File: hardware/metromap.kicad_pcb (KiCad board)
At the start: 4 copper layers, 100 x 100 mm, 160 parts, among them J1 USB_C_Receptacle_USB2.0_16P, U1 AZ1117-3.3, U2 SN74LVC1G125DBV, U3 ESP32-C6-MINI-1-H4

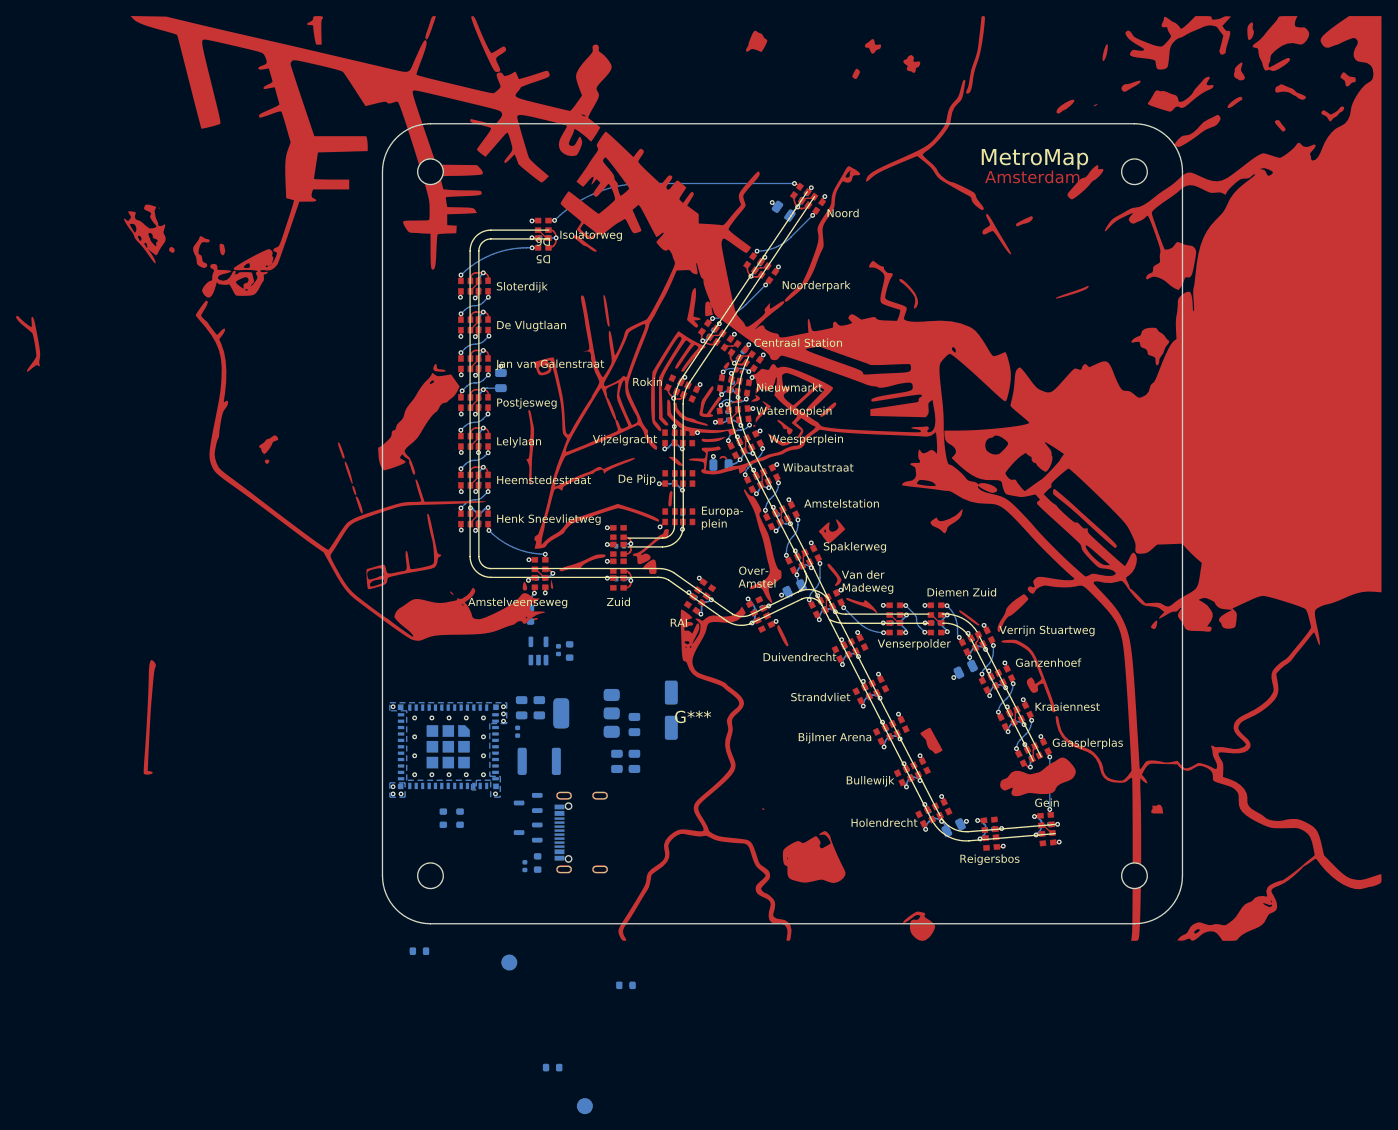
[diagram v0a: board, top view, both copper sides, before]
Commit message: Updated LED footprint
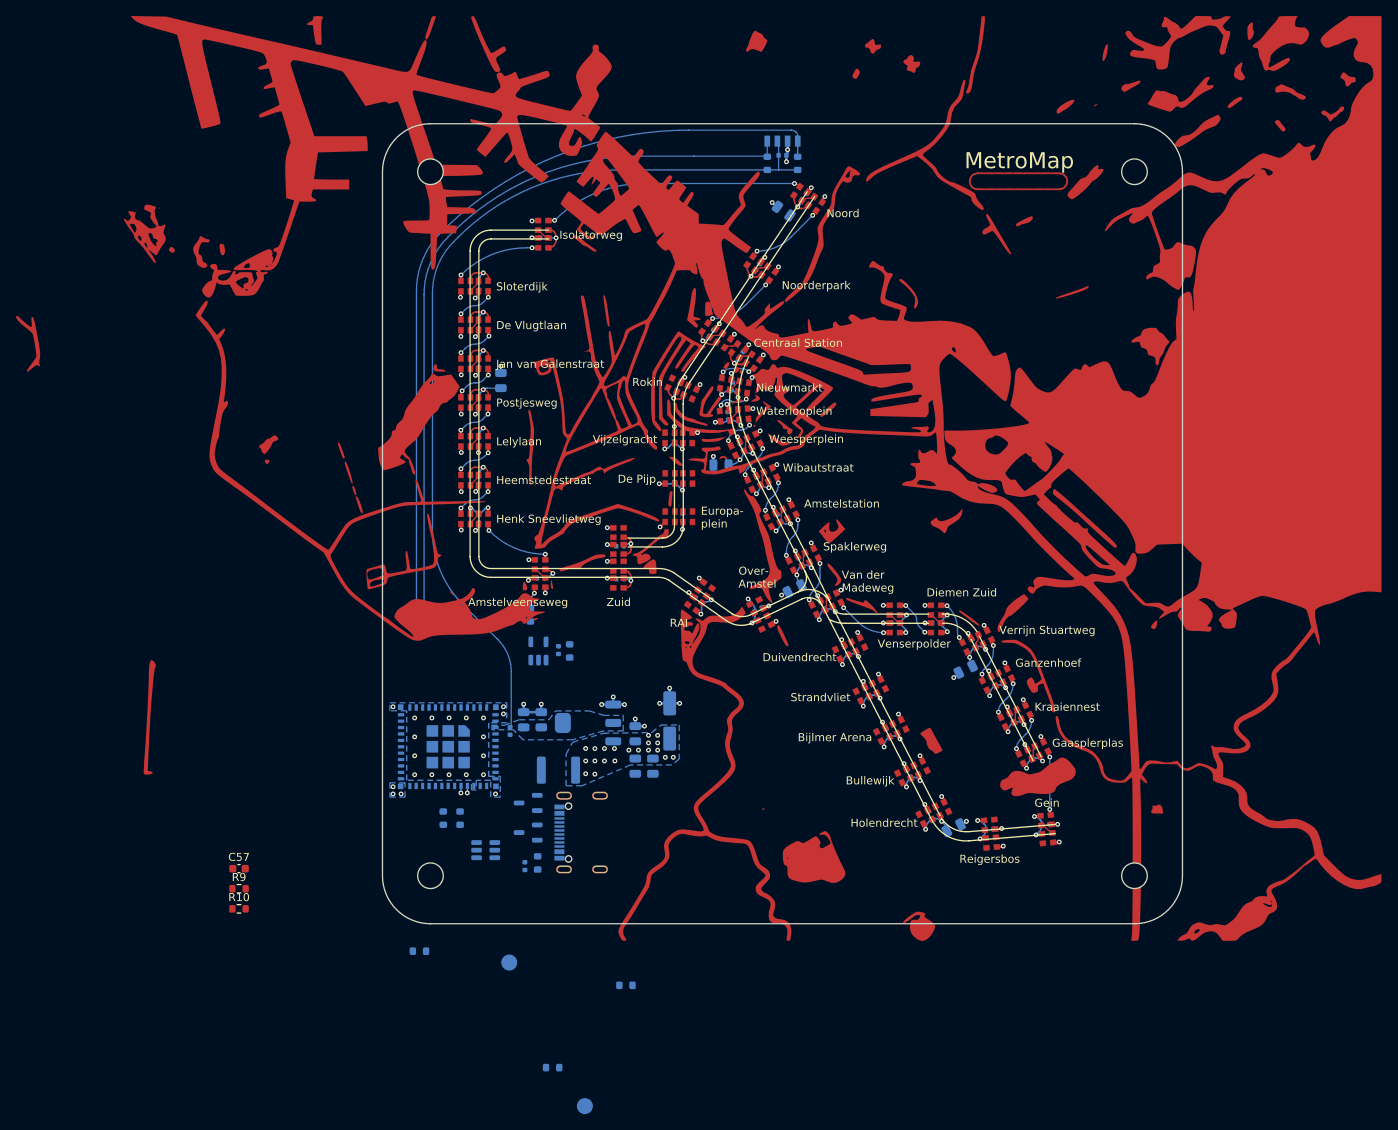
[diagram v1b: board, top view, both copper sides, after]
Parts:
- added C57: 1u, Capacitor_SMD:C_0603_1608Metric, F.Cu at (44.3, 122.1)
- added C58: 100n, Capacitor_SMD:C_0402_1005Metric, B.Cu at (112.2, 33.0)
- added R10: 10k, Resistor_SMD:R_0603_1608Metric, F.Cu at (44.3, 127.1)
- added R11: 4k7, Resistor_SMD:R_0603_1608Metric, B.Cu at (114.1, 34.0)
- added R12: 4k7, Resistor_SMD:R_0603_1608Metric, B.Cu at (110.3, 34.0)
- added R9: 1k, Resistor_SMD:R_0603_1608Metric, F.Cu at (44.3, 124.6)
- added U4: CH221K, Package_TO_SOT_SMD:SOT-23-6, B.Cu at (75.1, 119.8)
- added U5: VEML7700-TR, metro-tracker:XDCR_VEML7700-TR, B.Cu at (112.2, 30.5)
- moved F1 2.64 mm to (84.2, 109.8)
- moved C10 2.38 mm to (93.8, 109.3)
- moved C9 2.38 mm to (96.0, 109.3)
- moved C11 1.52 mm to (79.8, 103.5)
- moved C12 1.52 mm to (82.0, 103.5)
- moved C8 1.36 mm to (98.1, 103.7)
- moved U1 1.22 mm to (87.9, 103.9)
- moved C5 1.15 mm to (93.8, 105.2)
- moved C13 0.96 mm to (78.2, 104.9)
- turned D10 to 90 degrees
- turned D11 to -125 degrees
- turned D12 to -64 degrees
- turned D13 to -90 degrees
- turned D14 to -64 degrees
- turned D15 to -175 degrees
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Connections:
- D10 pad 1: GND -> +5V
- D10 pad 3: +5V -> GND
- D11 pad 1: GND -> +5V
- D11 pad 3: +5V -> GND
- D12 pad 1: GND -> +5V
- D12 pad 3: +5V -> GND
- D13 pad 1: GND -> +5V
- D13 pad 3: +5V -> GND
- D14 pad 1: GND -> +5V
- D14 pad 3: +5V -> GND
- D15 pad 1: GND -> +5V
- D15 pad 3: +5V -> GND
- D16 pad 1: GND -> +5V
- D16 pad 2: Net-(D16-DIN) -> unconnected-(D16-DOUT-Pad2)
- D16 pad 3: +5V -> GND
- D16 pad 4: unconnected-(D16-DOUT-Pad4) -> Net-(D16-DIN)
- D17 pad 1: GND -> +5V
- D17 pad 3: +5V -> GND
- D18 pad 1: GND -> +5V
- D18 pad 3: +5V -> GND
- D19 pad 1: GND -> +5V
- D19 pad 2: Net-(D19-DIN) -> Net-(D16-DIN)
- D19 pad 3: +5V -> GND
- D19 pad 4: Net-(D16-DIN) -> Net-(D19-DOUT)
- D20 pad 1: GND -> +5V
- D20 pad 2: Net-(D10-DOUT) -> Net-(D20-DIN)
- D20 pad 3: +5V -> GND
- D20 pad 4: Net-(D20-DOUT) -> Net-(D10-DIN)
- D21 pad 1: GND -> +5V
- D21 pad 2: Net-(D20-DOUT) -> Net-(D21-DIN)
- D21 pad 3: +5V -> GND
- D21 pad 4: Net-(D21-DOUT) -> Net-(D20-DIN)
- D22 pad 1: GND -> +5V
- D22 pad 2: Net-(D11-DOUT) -> Net-(D22-DIN)
- D22 pad 3: +5V -> GND
- D22 pad 4: Net-(D22-DOUT) -> Net-(D11-DIN)
- D23 pad 1: GND -> +5V
- D23 pad 2: Net-(D22-DOUT) -> Net-(D23-DIN)
- D23 pad 3: +5V -> GND
- D23 pad 4: Net-(D23-DOUT) -> Net-(D22-DIN)
- D24 pad 1: GND -> +5V
- D24 pad 2: Net-(D23-DOUT) -> Net-(D24-DIN)
- D24 pad 3: +5V -> GND
- D24 pad 4: Net-(D24-DOUT) -> Net-(D23-DIN)
- D25 pad 1: GND -> +5V
- D25 pad 2: Net-(D21-DOUT) -> Net-(D25-DIN)
- D25 pad 3: +5V -> GND
- D25 pad 4: Net-(D25-DOUT) -> Net-(D21-DIN)
- D26 pad 1: GND -> +5V
- D26 pad 2: Net-(D25-DOUT) -> Net-(D26-DIN)
- D26 pad 3: +5V -> GND
- D26 pad 4: Net-(D26-DOUT) -> Net-(D25-DIN)
- D27 pad 1: GND -> +5V
- D27 pad 3: +5V -> GND
- D28 pad 1: GND -> +5V
- D28 pad 3: +5V -> GND
- D29 pad 1: GND -> +5V
- D29 pad 2: Net-(D24-DOUT) -> Net-(D27-DOUT)
- D29 pad 3: +5V -> GND
- D29 pad 4: Net-(D27-DIN) -> Net-(D24-DIN)
- D3 pad 1: GND -> +5V
- D3 pad 3: +5V -> GND
- D30 pad 1: GND -> +5V
- D30 pad 3: +5V -> GND
- D31 pad 1: GND -> +5V
- D31 pad 2: Net-(D26-DOUT) -> Net-(D31-DIN)
- D31 pad 3: +5V -> GND
- D31 pad 4: Net-(D31-DOUT) -> Net-(D26-DIN)
- D32 pad 1: GND -> +5V
- D32 pad 2: Net-(D31-DOUT) -> Net-(D32-DIN)
- D32 pad 3: +5V -> GND
- D32 pad 4: Net-(D32-DOUT) -> Net-(D31-DIN)
- D33 pad 1: GND -> +5V
- D33 pad 3: +5V -> GND
- D34 pad 1: GND -> +5V
- D34 pad 2: Net-(D27-DOUT) -> Net-(D33-DOUT)
- D34 pad 3: +5V -> GND
- D34 pad 4: Net-(D33-DIN) -> Net-(D27-DIN)
- D35 pad 1: GND -> +5V
- D35 pad 3: +5V -> GND
- D36 pad 1: GND -> +5V
- D36 pad 3: +5V -> GND
- D37 pad 1: GND -> +5V
- D37 pad 3: +5V -> GND
- D38 pad 1: GND -> +5V
- D38 pad 3: +5V -> GND
- D39 pad 1: GND -> +5V
- D39 pad 2: Net-(D38-DOUT) -> Net-(D39-DIN)
- D39 pad 3: +5V -> GND
- D39 pad 4: Net-(D39-DOUT) -> Net-(D38-DIN)
- D4 pad 1: GND -> +5V
- D4 pad 2: Net-(D3-DOUT) -> Net-(D4-DIN)
- D4 pad 3: +5V -> GND
- D4 pad 4: Net-(D4-DOUT) -> Net-(D3-DIN)
- D40 pad 1: GND -> +5V
- D40 pad 2: Net-(D35-DOUT) -> Net-(D12-DOUT)
- D40 pad 3: +5V -> GND
- D40 pad 4: Net-(D12-DIN) -> Net-(D35-DIN)
- D41 pad 1: GND -> +5V
- D41 pad 3: +5V -> GND
- D42 pad 1: GND -> +5V
- D42 pad 2: Net-(D39-DOUT) -> Net-(D42-DIN)
- D42 pad 3: +5V -> GND
- D42 pad 4: Net-(D42-DOUT) -> Net-(D39-DIN)
- D43 pad 1: GND -> +5V
- D43 pad 2: Net-(D42-DOUT) -> Net-(D43-DIN)
- D43 pad 3: +5V -> GND
- D43 pad 4: Net-(D43-DOUT) -> Net-(D42-DIN)
- D44 pad 1: GND -> +5V
- D44 pad 3: +5V -> GND
- D45 pad 1: GND -> +5V
- D45 pad 3: +5V -> GND
- D46 pad 1: GND -> +5V
- D46 pad 2: Net-(D12-DOUT) -> Net-(D41-DOUT)
- D46 pad 3: +5V -> GND
- D46 pad 4: Net-(D41-DIN) -> Net-(D12-DIN)
- D47 pad 1: GND -> +5V
- D47 pad 3: +5V -> GND
- D48 pad 1: GND -> +5V
- D48 pad 3: +5V -> GND
- D49 pad 1: GND -> +5V
- D49 pad 3: +5V -> GND
- D5 pad 1: GND -> +5V
- D5 pad 2: Net-(D43-DOUT) -> Net-(D5-DIN)
- D5 pad 3: +5V -> GND
- D5 pad 4: Net-(D5-DOUT) -> Net-(D43-DIN)
- D50 pad 1: GND -> +5V
- D50 pad 3: +5V -> GND
- D51 pad 1: GND -> +5V
- D51 pad 3: +5V -> GND
- D52 pad 1: GND -> +5V
- D52 pad 2: Net-(D41-DOUT) -> Net-(D49-DOUT)
- D52 pad 3: +5V -> GND
- D52 pad 4: Net-(D49-DIN) -> Net-(D41-DIN)
- D53 pad 1: GND -> +5V
- D53 pad 3: +5V -> GND
- D54 pad 1: GND -> +5V
- D54 pad 3: +5V -> GND
- D55 pad 1: GND -> +5V
- D55 pad 2: Net-(D54-DOUT) -> Net-(D55-DIN)
- D55 pad 3: +5V -> GND
- D55 pad 4: Net-(D55-DOUT) -> Net-(D54-DIN)
- D56 pad 1: GND -> +5V
- D56 pad 3: +5V -> GND
- D57 pad 1: GND -> +5V
- D57 pad 2: Net-(D57-DIN) -> Net-(D54-DOUT)
- D57 pad 3: +5V -> GND
- D57 pad 4: Net-(D54-DIN) -> Net-(D57-DOUT)
- D58 pad 1: GND -> +5V
- D58 pad 2: Net-(D55-DOUT) -> Net-(D58-DIN)
- D58 pad 3: +5V -> GND
- D58 pad 4: Net-(D58-DOUT) -> Net-(D55-DIN)
- D59 pad 1: GND -> +5V
- D59 pad 3: +5V -> GND
- D6 pad 1: GND -> +5V
- D6 pad 2: Net-(D5-DOUT) -> Net-(D3-DOUT)
- D6 pad 3: +5V -> GND
- D6 pad 4: Net-(D3-DIN) -> Net-(D5-DIN)
- D60 pad 1: GND -> +5V
- D60 pad 3: +5V -> GND
- D61 pad 1: GND -> +5V
- D61 pad 2: Net-(D58-DOUT) -> Net-(D59-DOUT)
- D61 pad 3: +5V -> GND
- D61 pad 4: Net-(D59-DIN) -> Net-(D58-DIN)
- D62 pad 1: GND -> +5V
- D62 pad 3: +5V -> GND
- D63 pad 1: GND -> +5V
- D63 pad 3: +5V -> GND
- D64 pad 1: GND -> +5V
- D64 pad 2: Net-(D59-DOUT) -> Net-(D63-DOUT)
- D64 pad 3: +5V -> GND
- D64 pad 4: Net-(D63-DIN) -> Net-(D59-DIN)
- D65 pad 1: GND -> +5V
- D65 pad 3: +5V -> GND
- D66 pad 1: GND -> +5V
- D66 pad 3: +5V -> GND
- D67 pad 1: GND -> +5V
- D67 pad 3: +5V -> GND
- D68 pad 1: GND -> +5V
- D68 pad 2: Net-(D63-DOUT) -> Net-(D67-DOUT)
- D68 pad 3: +5V -> GND
- D68 pad 4: Net-(D67-DIN) -> Net-(D63-DIN)
- D69 pad 1: GND -> +5V
- D69 pad 3: +5V -> GND
- D7 pad 1: GND -> +5V
- D7 pad 2: Net-(D4-DOUT) -> Net-(D7-DIN)
- D7 pad 3: +5V -> GND
- D7 pad 4: Net-(D7-DOUT) -> Net-(D4-DIN)
- D70 pad 1: GND -> +5V
- D70 pad 3: +5V -> GND
- D71 pad 1: GND -> +5V
- D71 pad 2: Net-(D49-DOUT) -> Net-(D71-DIN)
- D71 pad 3: +5V -> GND
- D71 pad 4: Net-(D71-DOUT) -> Net-(D49-DIN)
- D72 pad 1: GND -> +5V
- D72 pad 2: Net-(D33-DOUT) -> Net-(D35-DOUT)
- D72 pad 3: +5V -> GND
- D72 pad 4: Net-(D35-DIN) -> Net-(D33-DIN)
- D73 pad 1: GND -> +5V
- D73 pad 2: Net-(D32-DOUT) -> Net-(D73-DIN)
- D73 pad 3: +5V -> GND
- D73 pad 4: Net-(D73-DOUT) -> Net-(D32-DIN)
- D74 pad 1: GND -> +5V
- D74 pad 2: Net-(D73-DOUT) -> Net-(D38-DOUT)
- D74 pad 3: +5V -> GND
- D74 pad 4: Net-(D38-DIN) -> Net-(D73-DIN)
- D75 pad 1: GND -> +5V
- D75 pad 2: Net-(D67-DOUT) -> Net-(D75-DIN)
- D75 pad 3: +5V -> GND
- D75 pad 4: Net-(D75-DOUT) -> Net-(D67-DIN)
- D76 pad 1: GND -> +5V
- D76 pad 3: +5V -> GND
- D77 pad 1: GND -> +5V
- D77 pad 3: +5V -> GND
- D78 pad 1: GND -> +5V
- D78 pad 3: +5V -> GND
- D79 pad 1: GND -> +5V
- D79 pad 2: Net-(D71-DOUT) -> Net-(D57-DOUT)
- D79 pad 3: +5V -> GND
- D79 pad 4: Net-(D57-DIN) -> Net-(D71-DIN)
- D8 pad 1: GND -> +5V
- D8 pad 2: Net-(D7-DOUT) -> Net-(D11-DOUT)
- D8 pad 3: +5V -> GND
- D8 pad 4: Net-(D11-DIN) -> Net-(D7-DIN)
- D80 pad 1: GND -> +5V
- D80 pad 3: +5V -> GND
- D81 pad 1: GND -> +5V
- D81 pad 2: Net-(D75-DOUT) -> Net-(D19-DOUT)
- D81 pad 3: +5V -> GND
- D81 pad 4: Net-(D19-DIN) -> Net-(D75-DIN)
- D82 pad 1: GND -> +5V
- D82 pad 2: /LEDs/DATA_IN -> Net-(D50-DOUT)
- D82 pad 3: +5V -> GND
- D82 pad 4: Net-(D50-DIN) -> /LEDs/DATA_IN
- D83 pad 1: GND -> +5V
- D83 pad 3: +5V -> GND
- D84 pad 1: GND -> +5V
- D84 pad 3: +5V -> GND
- D9 pad 1: GND -> +5V
- D9 pad 2: Net-(D50-DOUT) -> Net-(D10-DOUT)
- D9 pad 3: +5V -> GND
- D9 pad 4: Net-(D10-DIN) -> Net-(D50-DIN)
- U3 pad 15: unconnected-(U3-IO6-Pad15) -> /SDA
- U3 pad 16: unconnected-(U3-IO7-Pad16) -> /SCL
- U3 pad 29: unconnected-(U3-IO23-Pad29) -> /TOUCH
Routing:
- net +3.3V: track 0.00 -> 113.6 mm
- net /SDA: track 0.00 -> 102.4 mm, vias 0 -> 1
- net /SCL: track 0.00 -> 95.3 mm, vias 0 -> 1
- net Net-(D3-DOUT): track 1.65 -> 32.7 mm, vias 0 -> 2
- net Net-(D3-DIN): track 32.7 -> 1.65 mm, vias 2 -> 0
- net GND: track 104.8 -> 121.9 mm, vias 106 -> 117
- net Net-(D43-DOUT): track 11.2 -> 0.00 mm, vias 2 -> 0
- net Net-(D43-DIN): track 0.00 -> 11.2 mm, vias 0 -> 2
- net Net-(D4-DOUT): track 10.1 -> 0.00 mm, vias 2 -> 0
- net Net-(D4-DIN): track 0.00 -> 10.1 mm, vias 0 -> 2
- net Net-(D19-DOUT): track 0.00 -> 8.04 mm, vias 0 -> 2
- net Net-(D19-DIN): track 8.04 -> 0.00 mm, vias 2 -> 0
- net Net-(D11-DOUT): track 1.74 -> 9.67 mm, vias 0 -> 2
- net Net-(D11-DIN): track 9.67 -> 1.74 mm, vias 2 -> 0
- net Net-(D57-DOUT): track 0.00 -> 7.73 mm, vias 0 -> 2
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- added copper zone on B.Cu, net +3.3V
- added copper zone on B.Cu, net +5V
- added copper zone on F.Cu, net /TOUCH

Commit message: replaced buffer
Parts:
- added TP3: ~, TestPoint:TestPoint_Pad_D2.0mm, B.Cu at (83.8, 91.2)
- added TP4: ~, TestPoint:TestPoint_Pad_D2.0mm, B.Cu at (88.2, 95.7)
- C57, R10, R9: moved to B.Cu
- U2: value SN74LVC1G125DBV -> SN74AHCT1G125DBVR
- moved R1 38.7 mm to (79.0, 108.5)
- moved C57 35.3 mm to (79.3, 125.5)
- moved R9 35.1 mm to (79.3, 123.8), turned to 180 degrees
- moved R10 31.8 mm to (75.9, 123.8), turned to 180 degrees
- moved TP2 26.7 mm to (90.5, 125.2)
- moved R3 19.8 mm to (80.6, 121.0), turned to -90 degrees
- moved R4 16.7 mm to (79.0, 121.0), turned to -90 degrees
- moved TP1 9.82 mm to (82.8, 125.2)
- moved C15 8.54 mm to (88.0, 124.7), turned to -90 degrees
- moved R8 6.14 mm to (86.7, 124.9), turned to -90 degrees
- moved R7 4.90 mm to (74.7, 116.2), turned to 180 degrees
- moved R5 3.02 mm to (74.7, 114.7), turned to 180 degrees
- moved U4 1.47 mm to (76.0, 121.0)
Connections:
- net /~{OE_EN} renamed /~{OE}
- D2 pad 1: Net-(D2-K-Pad1) -> /CON_USB_D-
- D2 pad 2: Net-(D2-K-Pad2) -> /CON_USB_D+
- J1 pad A6: Net-(D2-K-Pad1) -> /CON_USB_D+
- J1 pad A7: Net-(D2-K-Pad2) -> /CON_USB_D-
- J1 pad B6: Net-(D2-K-Pad1) -> /CON_USB_D+
- J1 pad B7: Net-(D2-K-Pad2) -> /CON_USB_D-
- R5 pad 1: Net-(D2-K-Pad2) -> /CON_USB_D-
- R7 pad 1: Net-(D2-K-Pad1) -> /CON_USB_D+
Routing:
- net /SDA: track 102.4 -> 131.2 mm, vias 1 -> 2
- net /~{OE}: track 0.00 -> 27.8 mm, vias 0 -> 2
- net /SCL: track 95.3 -> 121.8 mm, vias 1 -> 2
- net Net-(D1-K-Pad1): track 0.00 -> 24.8 mm
- net /LED_DATA: track 0.00 -> 22.0 mm, vias 0 -> 2
- net GND: track 121.9 -> 141.1 mm, vias 117 -> 133
- net /CON_USB_D+: track 0.00 -> 13.6 mm
- net /CON_USB_D-: track 0.00 -> 12.7 mm
- net Net-(J1-CC1): track 0.00 -> 9.36 mm, vias 0 -> 2
- net Net-(U4-VDD): track 0.00 -> 7.98 mm
- net Net-(J1-CC2): track 0.00 -> 7.92 mm
- net /USB_D+: track 0.00 -> 6.76 mm
- net /USB_D-: track 0.00 -> 5.96 mm
- net Net-(R6-Pad1): track 0.00 -> 5.58 mm
- net +3.3V: track 113.6 -> 117.8 mm
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- removed copper zone on F.Cu, net /TOUCH
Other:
- board text added: "DATA_IN"
- board text added: "Europa plein"
- board text added: "GND"
- board text added: "Over amstel"
- board text added: "VBUS"
- board text added: "~{OE}"
- board text removed: "Europa- plein"
- board text removed: "Over- Amstel"

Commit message: Initial routing done
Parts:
- added C59: 47u, Capacitor_SMD:CP_Elec_6.3x7.7, B.Cu at (101.6, 105.8)
- C8: footprint Capacitor_SMD:CP_Elec_5x5.7 -> Capacitor_SMD:CP_Elec_6.3x7.7
- moved C8 6.14 mm to (101.6, 98.6), turned to 0 degrees
- moved C2 3.42 mm to (134.0, 113.6), turned to -64 degrees
- moved TP2 2.55 mm to (93.0, 125.2)
- moved D60 2.33 mm to (119.5, 95.1), turned to 116 degrees
- moved D77 2.32 mm to (129.6, 109.6), turned to 116 degrees
- moved D14 2.31 mm to (132.2, 114.8), turned to 116 degrees
- moved D70 2.27 mm to (126.9, 104.5), turned to 116 degrees
- moved D18 2.26 mm to (130.2, 115.8), turned to 116 degrees
- moved D65 2.26 mm to (122.2, 100.3), turned to 116 degrees
- moved D78 2.23 mm to (101.3, 89.0), turned to 145 degrees
- moved D84 2.22 mm to (102.5, 87.2), turned to 145 degrees
- moved D69 2.22 mm to (124.9, 105.5), turned to 116 degrees
- moved D66 2.21 mm to (124.2, 99.3), turned to 116 degrees
- moved D76 2.20 mm to (127.5, 110.6), turned to 116 degrees
- moved D62 2.10 mm to (121.5, 94.2), turned to 116 degrees
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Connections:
- net Net-(D1-K-Pad1) renamed /VBUS
- net Net-(J1-SHIELD) renamed /SH
- D13 pad 2: unconnected-(D13-DOUT-Pad2) -> Net-(D13-DOUT)
- D13 pad 4: unconnected-(D13-DIN-Pad4) -> Net-(D13-DIN)
- D14 pad 2: unconnected-(D14-DOUT-Pad2) -> Net-(D14-DOUT)
- D14 pad 4: unconnected-(D14-DIN-Pad4) -> Net-(D14-DIN)
- D15 pad 2: unconnected-(D15-DOUT-Pad2) -> Net-(D15-DOUT)
- D15 pad 4: unconnected-(D15-DIN-Pad4) -> Net-(D15-DIN)
- D16 pad 2: unconnected-(D16-DOUT-Pad2) -> Net-(D15-DIN)
- D17 pad 2: unconnected-(D17-DOUT-Pad2) -> Net-(D14-DIN)
- D17 pad 4: unconnected-(D17-DIN-Pad4) -> Net-(D15-DOUT)
- D18 pad 2: unconnected-(D18-DOUT-Pad2) -> Net-(D18-DOUT)
- D18 pad 4: unconnected-(D18-DIN-Pad4) -> Net-(D14-DOUT)
- D28 pad 2: unconnected-(D28-DOUT-Pad2) -> Net-(D28-DOUT)
- D28 pad 4: unconnected-(D28-DIN-Pad4) -> Net-(D28-DIN)
- D30 pad 2: unconnected-(D30-DOUT-Pad2) -> Net-(D30-DOUT)
- D30 pad 4: unconnected-(D30-DIN-Pad4) -> Net-(D28-DOUT)
- D36 pad 2: unconnected-(D36-DOUT-Pad2) -> Net-(D36-DOUT)
- D36 pad 4: unconnected-(D36-DIN-Pad4) -> Net-(D30-DOUT)
- D37 pad 2: unconnected-(D37-DOUT-Pad2) -> Net-(D37-DOUT)
- D37 pad 4: unconnected-(D37-DIN-Pad4) -> Net-(D13-DOUT)
- D44 pad 2: unconnected-(D44-DOUT-Pad2) -> Net-(D44-DOUT)
- D44 pad 4: unconnected-(D44-DIN-Pad4) -> Net-(D37-DOUT)
- D45 pad 4: unconnected-(D45-DIN-Pad4) -> Net-(D44-DOUT)
- D47 pad 2: unconnected-(D47-DOUT-Pad2) -> Net-(D28-DIN)
- D47 pad 4: unconnected-(D47-DIN-Pad4) -> Net-(D47-DIN)
- D48 pad 2: unconnected-(D48-DOUT-Pad2) -> Net-(D47-DIN)
- D48 pad 4: unconnected-(D48-DIN-Pad4) -> Net-(D48-DIN)
- D51 pad 2: unconnected-(D51-DOUT-Pad2) -> Net-(D48-DIN)
- D51 pad 4: unconnected-(D51-DIN-Pad4) -> Net-(D51-DIN)
- D53 pad 2: unconnected-(D53-DOUT-Pad2) -> Net-(D51-DIN)
- D53 pad 4: unconnected-(D53-DIN-Pad4) -> Net-(D53-DIN)
- D56 pad 2: unconnected-(D56-DOUT-Pad2) -> Net-(D56-DOUT)
- D56 pad 4: unconnected-(D56-DIN-Pad4) -> Net-(D56-DIN)
- D60 pad 2: unconnected-(D60-DOUT-Pad2) -> Net-(D60-DOUT)
- D60 pad 4: unconnected-(D60-DIN-Pad4) -> Net-(D60-DIN)
- D62 pad 2: unconnected-(D62-DOUT-Pad2) -> Net-(D60-DIN)
- D62 pad 4: unconnected-(D62-DIN-Pad4) -> Net-(D62-DIN)
- D65 pad 2: unconnected-(D65-DOUT-Pad2) -> Net-(D62-DIN)
- D65 pad 4: unconnected-(D65-DIN-Pad4) -> Net-(D65-DIN)
- D66 pad 2: unconnected-(D66-DOUT-Pad2) -> Net-(D65-DIN)
- D66 pad 4: unconnected-(D66-DIN-Pad4) -> Net-(D66-DIN)
- D69 pad 2: unconnected-(D69-DOUT-Pad2) -> Net-(D66-DIN)
- D69 pad 4: unconnected-(D69-DIN-Pad4) -> Net-(D69-DIN)
- D70 pad 2: unconnected-(D70-DOUT-Pad2) -> Net-(D69-DIN)
- D70 pad 4: unconnected-(D70-DIN-Pad4) -> Net-(D70-DIN)
- D76 pad 2: unconnected-(D76-DOUT-Pad2) -> Net-(D70-DIN)
- D76 pad 4: unconnected-(D76-DIN-Pad4) -> Net-(D76-DIN)
- D77 pad 2: unconnected-(D77-DOUT-Pad2) -> Net-(D76-DIN)
- D77 pad 4: unconnected-(D77-DIN-Pad4) -> Net-(D18-DOUT)
- D78 pad 2: unconnected-(D78-DOUT-Pad2) -> Net-(D53-DIN)
- D78 pad 4: unconnected-(D78-DIN-Pad4) -> Net-(D78-DIN)
- D80 pad 2: unconnected-(D80-DOUT-Pad2) -> Net-(D56-DIN)
- D80 pad 4: unconnected-(D80-DIN-Pad4) -> Net-(D60-DOUT)
- D83 pad 2: unconnected-(D83-DOUT-Pad2) -> Net-(D13-DIN)
- D83 pad 4: unconnected-(D83-DIN-Pad4) -> Net-(D36-DOUT)
- D84 pad 2: unconnected-(D84-DOUT-Pad2) -> Net-(D78-DIN)
- D84 pad 4: unconnected-(D84-DIN-Pad4) -> Net-(D56-DOUT)
- U3 pad 29: /TOUCH -> unconnected-(U3-IO23-Pad29)
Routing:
- net Net-(D28-DIN): track 0.00 -> 22.3 mm, vias 0 -> 2
- net GND: track 141.1 -> 161.4 mm, vias 133 -> 145
- net Net-(D60-DOUT): track 0.00 -> 13.1 mm, vias 0 -> 2
- net Net-(D53-DIN): track 0.00 -> 11.5 mm, vias 0 -> 2
- net Net-(D56-DOUT): track 0.00 -> 8.94 mm, vias 0 -> 2
- net /VBUS: track 24.8 -> 16.4 mm
- net Net-(D30-DOUT): track 0.00 -> 7.41 mm, vias 0 -> 2
- net Net-(D15-DIN): track 0.00 -> 7.21 mm, vias 0 -> 2
- net Net-(D14-DIN): track 0.00 -> 6.88 mm, vias 0 -> 2
- net Net-(D70-DIN): track 0.00 -> 6.11 mm, vias 0 -> 2
- net Net-(D18-DOUT): track 0.00 -> 6.07 mm, vias 0 -> 2
- net Net-(D66-DIN): track 0.00 -> 5.98 mm, vias 0 -> 2
- net Net-(D62-DIN): track 0.00 -> 5.94 mm, vias 0 -> 2
- net Net-(D13-DIN): track 0.00 -> 5.60 mm, vias 0 -> 2
- net Net-(D37-DOUT): track 0.00 -> 5.59 mm, vias 0 -> 2
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- added copper zone on B.Cu, net /SH
- added copper zone on B.Cu, net /VBUS
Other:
- board text added: "ESP32-C6-MINI"
- board text added: "MetroMap Amsterdam V1.0"
- board text added: "PATCH ANTENNA"
